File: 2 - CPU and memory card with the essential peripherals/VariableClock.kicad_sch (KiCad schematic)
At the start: 30 parts, among them SW1 BOOT LO, SW2 BOOT HI, U1 74AC74, U2 74AC74, U3 74AC74, U4 74AC08, U5 74HC251, X1 10MHz, X2 1.8432MHz, X3 8MHz

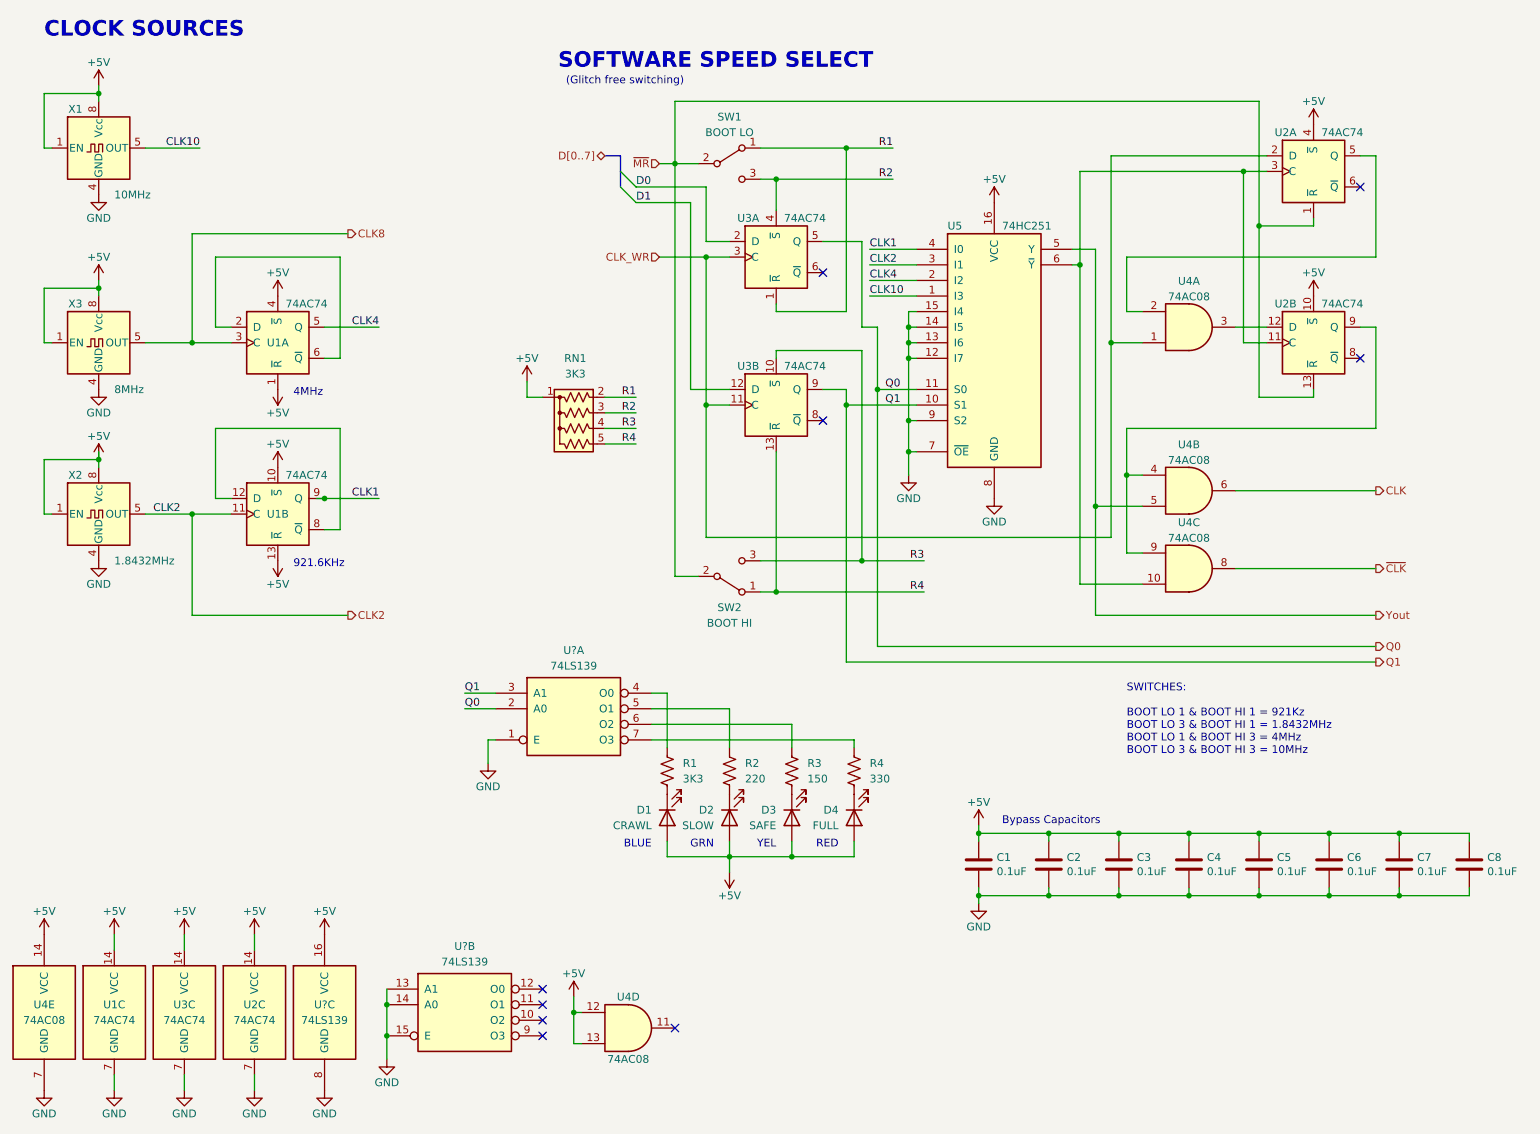
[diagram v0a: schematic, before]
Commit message: Removed unessential components and added capacitors on the bus lanes. Still need work for on the silkscreen side.
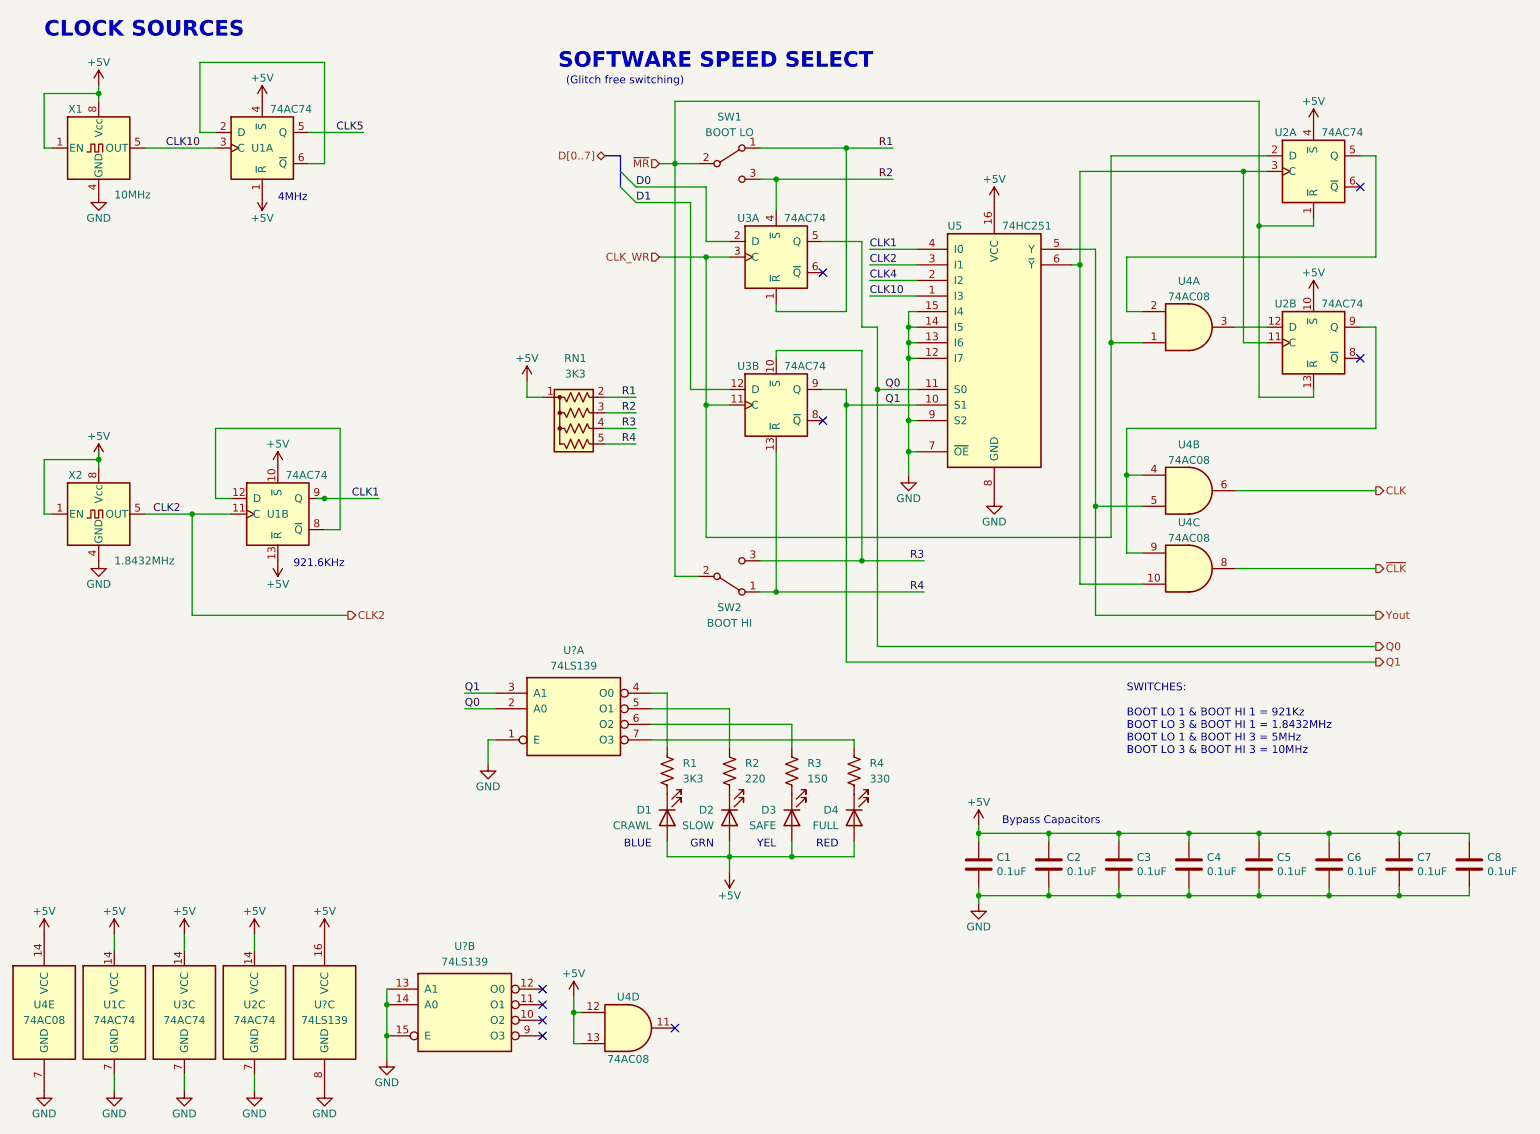
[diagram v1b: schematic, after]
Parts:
- removed X3: 8MHz, 0_Library:DIP-8-4_W7.62mm_Oscillator_Socket, symbol Oscillator:CXO_DIP8
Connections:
- net CLK8 is gone; now on net CLK10: U1.3 (C)
- net CLK4: no longer U1.5 (Q)
- new net CLK5: U1.5 (Q)
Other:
- note added: "SWITCHES: BOOT LO 1 & BOOT HI 1 = 921Kz BOOT LO 3 & BOOT HI 1 = 1.8432MHz BOOT LO 1 & BOOT HI 3 = 5MHz BOOT LO 3 & BOOT HI 3 = 10MHz"
- note removed: "SWITCHES: BOOT LO 1 & BOOT HI 1 = 921Kz BOOT LO 3 & BOOT HI 1 = 1.8432MHz BOOT LO 1 & BOOT HI 3 = 4MHz BOOT LO 3 & BOOT HI 3 = 10MHz"
- moved on the sheet: U1A
